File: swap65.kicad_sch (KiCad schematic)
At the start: 0 parts

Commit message: wired up first pass of schematic
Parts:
- added C1, C15, C16, C7: 1uF, symbol Device:C_Small
- added C10, C11, C12, C13, C14, C17, C2, C5, C8, C9: 100nF, symbol Device:C_Small
- added C3, C4: 22pF, symbol Device:C_Small
- added C6: 10uF, symbol Device:C_Small
- added F1: 500mA, symbol Device:Polyfuse_Small
- added J1: SWD, symbol Connector_Generic:Conn_01x05
- added J2: USB_C_Receptacle_USB2.0, symbol Connector:USB_C_Receptacle_USB2.0
- added R1, R2: 27R, symbol Device:R_Small
- added R3, R4, R5, R8: 1k, symbol Device:R_Small
- added R6, R7: 5k1, symbol Device:R_Small
- added SW1: SW_Push, symbol Switch:SW_Push
- added U1: RP2040, Package_DFN_QFN:QFN-56-1EP_7x7mm_P0.4mm_EP3.2x3.2mm, symbol MCU_RaspberryPi:RP2040
- added U2: USBLC6-2SC6, Package_TO_SOT_SMD:SOT-23-6, symbol Power_Protection:USBLC6-2SC6
- added U3: XC6206PxxxMR, Package_TO_SOT_SMD:SOT-23-3, symbol Regulator_Linear:XC6206PxxxMR
- added U4: W25Q128JVS, Package_SO:SOIC-8_5.23x5.23mm_P1.27mm, symbol Memory_Flash:W25Q128JVS
- added Y1: 12MHz, symbol Device:Crystal_GND24_Small
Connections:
- new net: C4.2, R4.1, Y1.1
- new net: C3.2, U1.20 (XIN), Y1.3
- new net: J2.S1 (SHIELD), R5.2
- new net: R4.2, U1.21 (XOUT)
- new net +1V1: C1.1, C2.1, C5.1, U1.23 (DVDD), U1.45 (VREG_VOUT), U1.50 (DVDD)
- new net +3V3: C10.1, C11.1, C12.1, C13.1, C14.1, C16.2, C17.1, C6.1, C7.1, C8.1, C9.1, J1.2 (Pin_2), R3.1, U1.1 (IOVDD), U1.10 (IOVDD), U1.22 (IOVDD), U1.33 (IOVDD), U1.42 (IOVDD), U1.43 (ADC_AVDD), U1.44 (VREG_IN), U1.48 (USB_VDD), U1.49 (IOVDD), U3.2 (VO), U4.8 (VCC)
- new net +5V: C15.2, F1.2, U2.5 (VBUS), U3.3 (VI)
- new net CC1: J2.A5 (CC1), R6.1
- new net CC2: J2.B5 (CC2), R7.1
- new net CS: R8.2, U1.56 (QSPI_SS), U4.1 (~{CS})
- new net D_+: R1.2, U1.47 (USB_DP)
- new net D_-: R2.2, U1.46 (USB_DM)
- new net D_N: R2.1, U2.3 (I/O2)
- new net D_P: R1.1, U2.1 (I/O1)
- new net D_USB_N: J2.A7 (D-), J2.B7 (D-), U2.4 (I/O2)
- new net D_USB_P: J2.A6 (D+), J2.B6 (D+), U2.6 (I/O1)
- new net GND: C1.2, C10.2, C11.2, C12.2, C13.2, C14.2, C15.1, C16.1, C17.2, C2.2, C3.1, C4.1, C5.2, C6.2, C7.2, C8.2, C9.2, J1.3 (Pin_3), J2.A1 (GND), J2.A12 (GND), J2.B1 (GND), J2.B12 (GND), R5.1, R6.2, R7.2, SW1.1, U1.19 (TESTEN), U1.57 (GND), U2.2 (GND), U3.1 (GND), U4.4 (GND), Y1.2, Y1.4
- new net QSPI_CLK: U1.52 (QSPI_SCLK), U4.6 (CLK)
- new net RESET: J1.1 (Pin_1), R3.2, U1.26 (RUN)
- new net SD0: U1.53 (QSPI_SD0), U4.5 (DI(IO0))
- new net SD1: U1.55 (QSPI_SD1), U4.2 (DO(IO1))
- new net SD2: U1.54 (QSPI_SD2), U4.3 (IO2)
- new net SD3: U1.51 (QSPI_SD3), U4.7 (IO3)
- new net SWCLK: J1.5 (Pin_5), U1.24 (SWCLK)
- new net SWD: J1.4 (Pin_4), U1.25 (SWD)
- new net USB_BOOT: R8.1, SW1.2
- new net VBUS: F1.1, J2.A4 (VBUS), J2.A9 (VBUS), J2.B4 (VBUS), J2.B9 (VBUS)
- no-connect marks 0 -> 2
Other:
- added sheet matrix (matrix.kicad_sch)
- title: (none) -> Swap 65 PCB

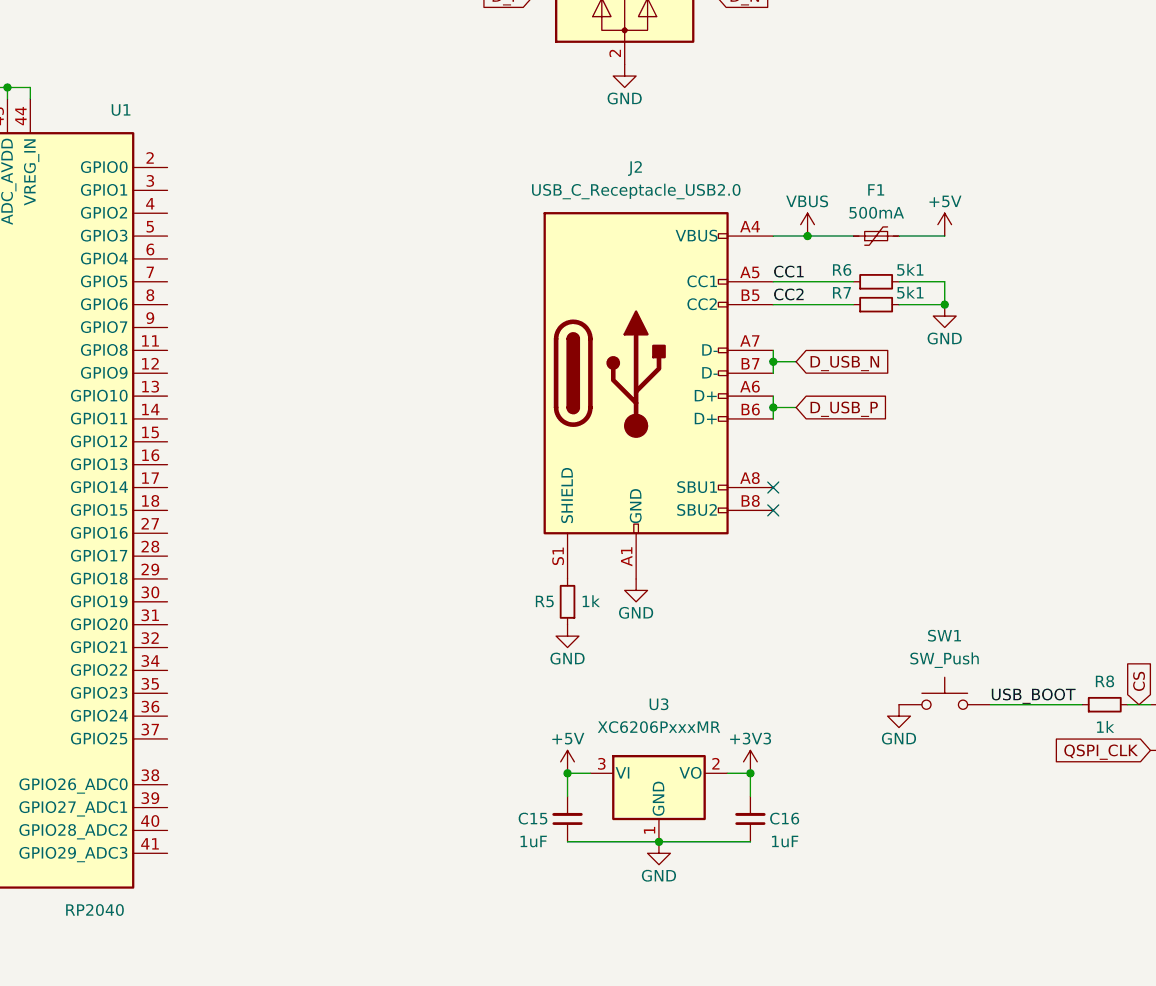
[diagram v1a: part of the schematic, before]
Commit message: did initial routing of MCU and USB
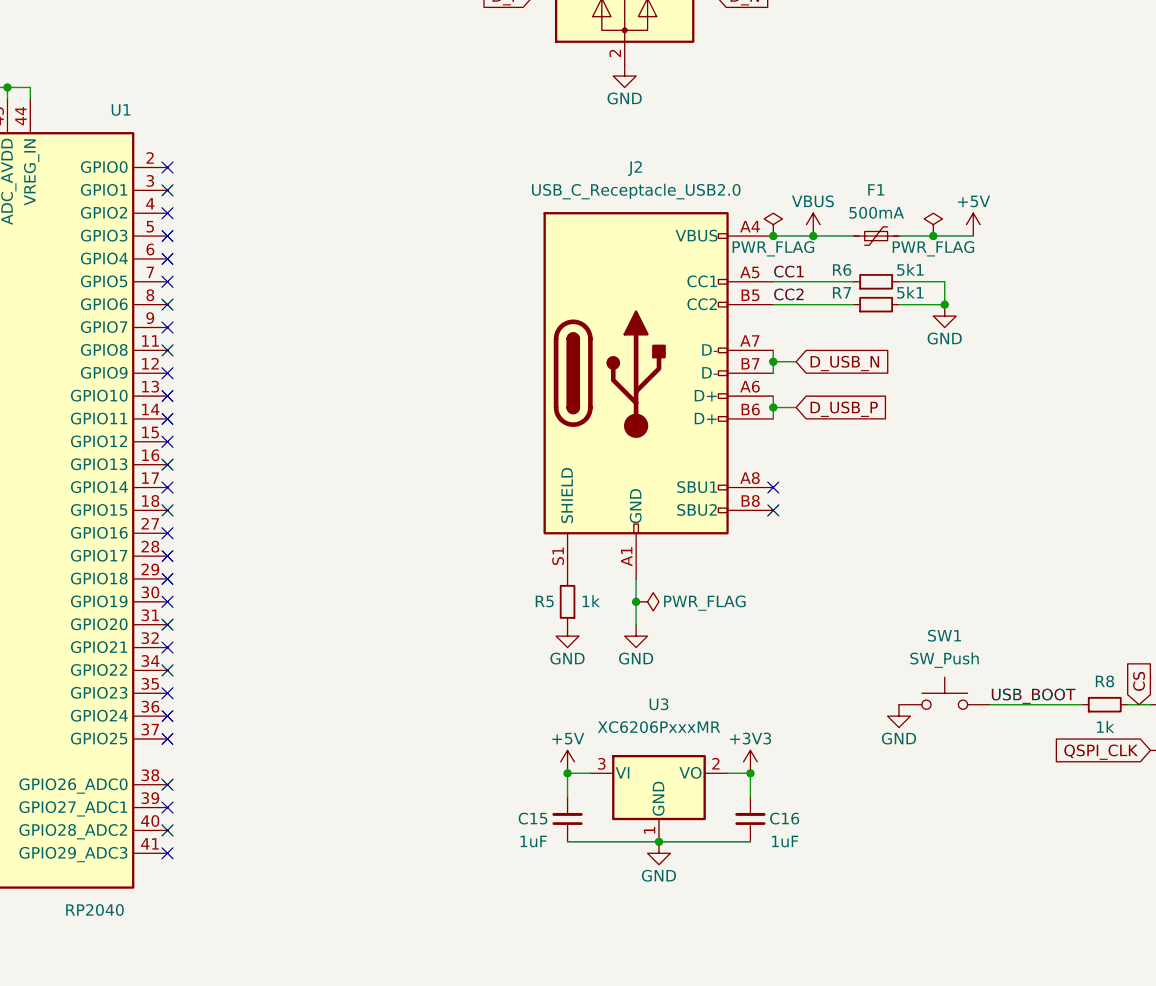
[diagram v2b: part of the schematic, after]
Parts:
- C1, C10, C11, C12, C13, C14, C15, C16, C17, C2, C3, C4, C5, C6, C7, C8, C9: footprint (none) -> Capacitor_SMD:C_0402_1005Metric_Pad0.74x0.62mm_HandSolder
- F1: footprint (none) -> Fuse:Fuse_0805_2012Metric_Pad1.15x1.40mm_HandSolder
- J1: footprint (none) -> Connector_PinHeader_2.54mm:PinHeader_1x05_P2.54mm_Vertical
- J2: footprint (none) -> Connector_USB:USB_C_Receptacle_HRO_TYPE-C-31-M-12
- R1, R2, R3, R4, R5, R6, R7, R8: footprint (none) -> Resistor_SMD:R_0402_1005Metric_Pad0.72x0.64mm_HandSolder
- SW1: footprint (none) -> Button_Switch_SMD:SW_SPST_SKQG_WithStem
- Y1: footprint (none) -> Crystal:Crystal_SMD_2016-4Pin_2.0x1.6mm
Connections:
- no-connect marks 2 -> 32

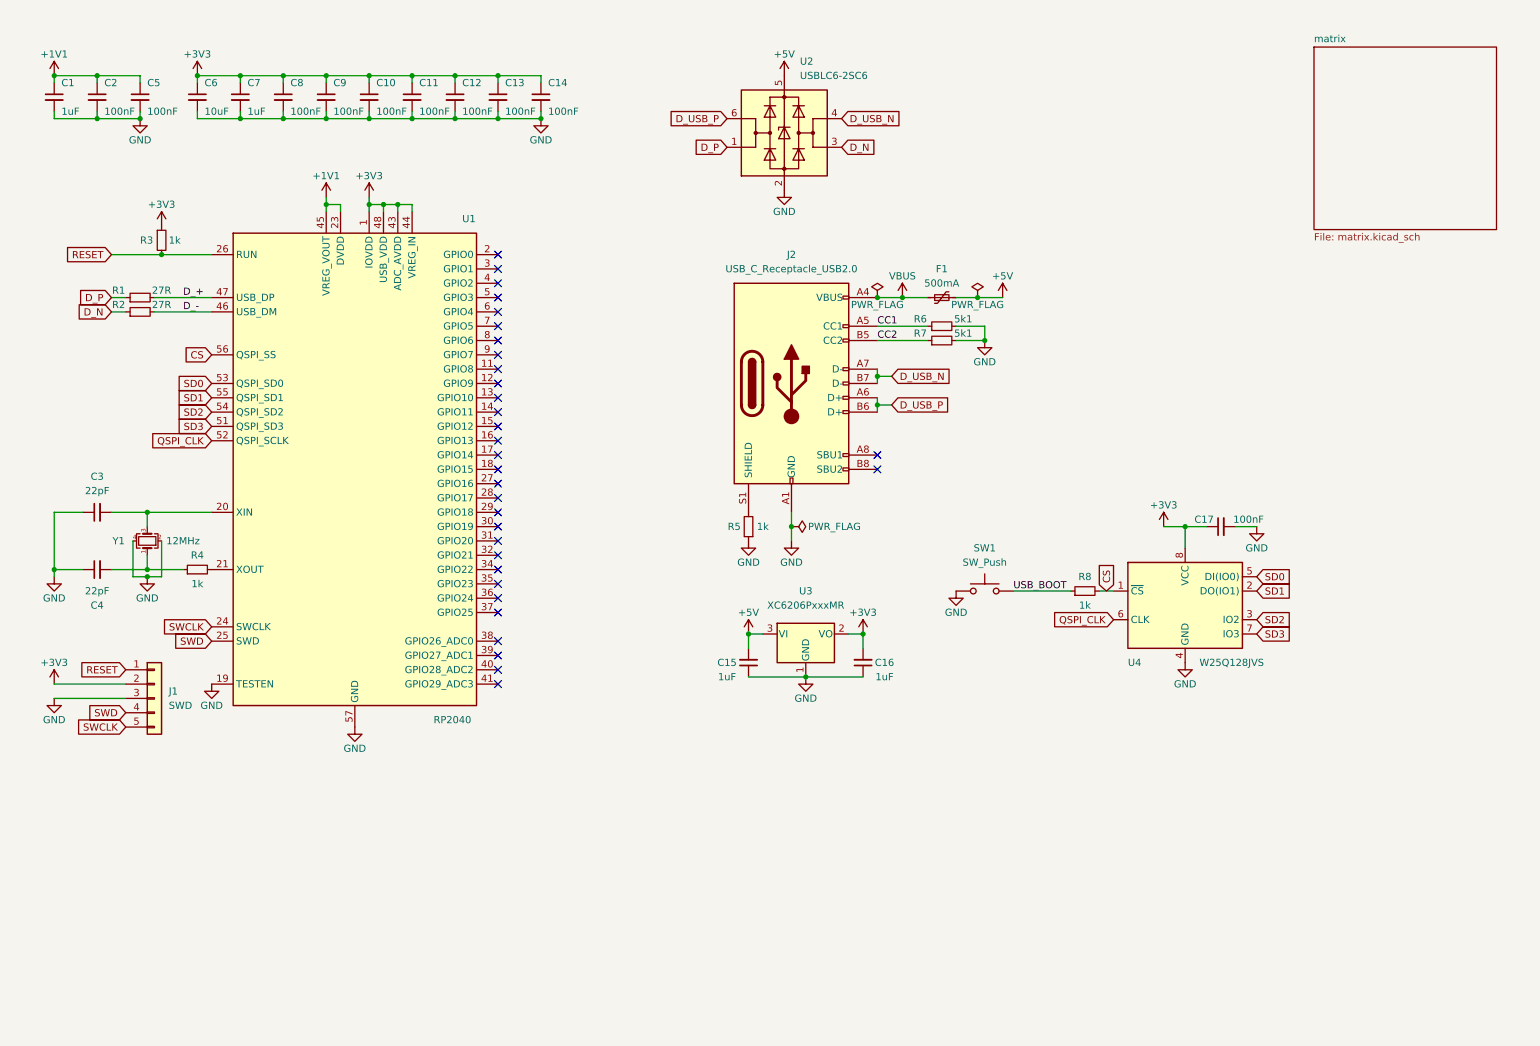
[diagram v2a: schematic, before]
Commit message: routed columns
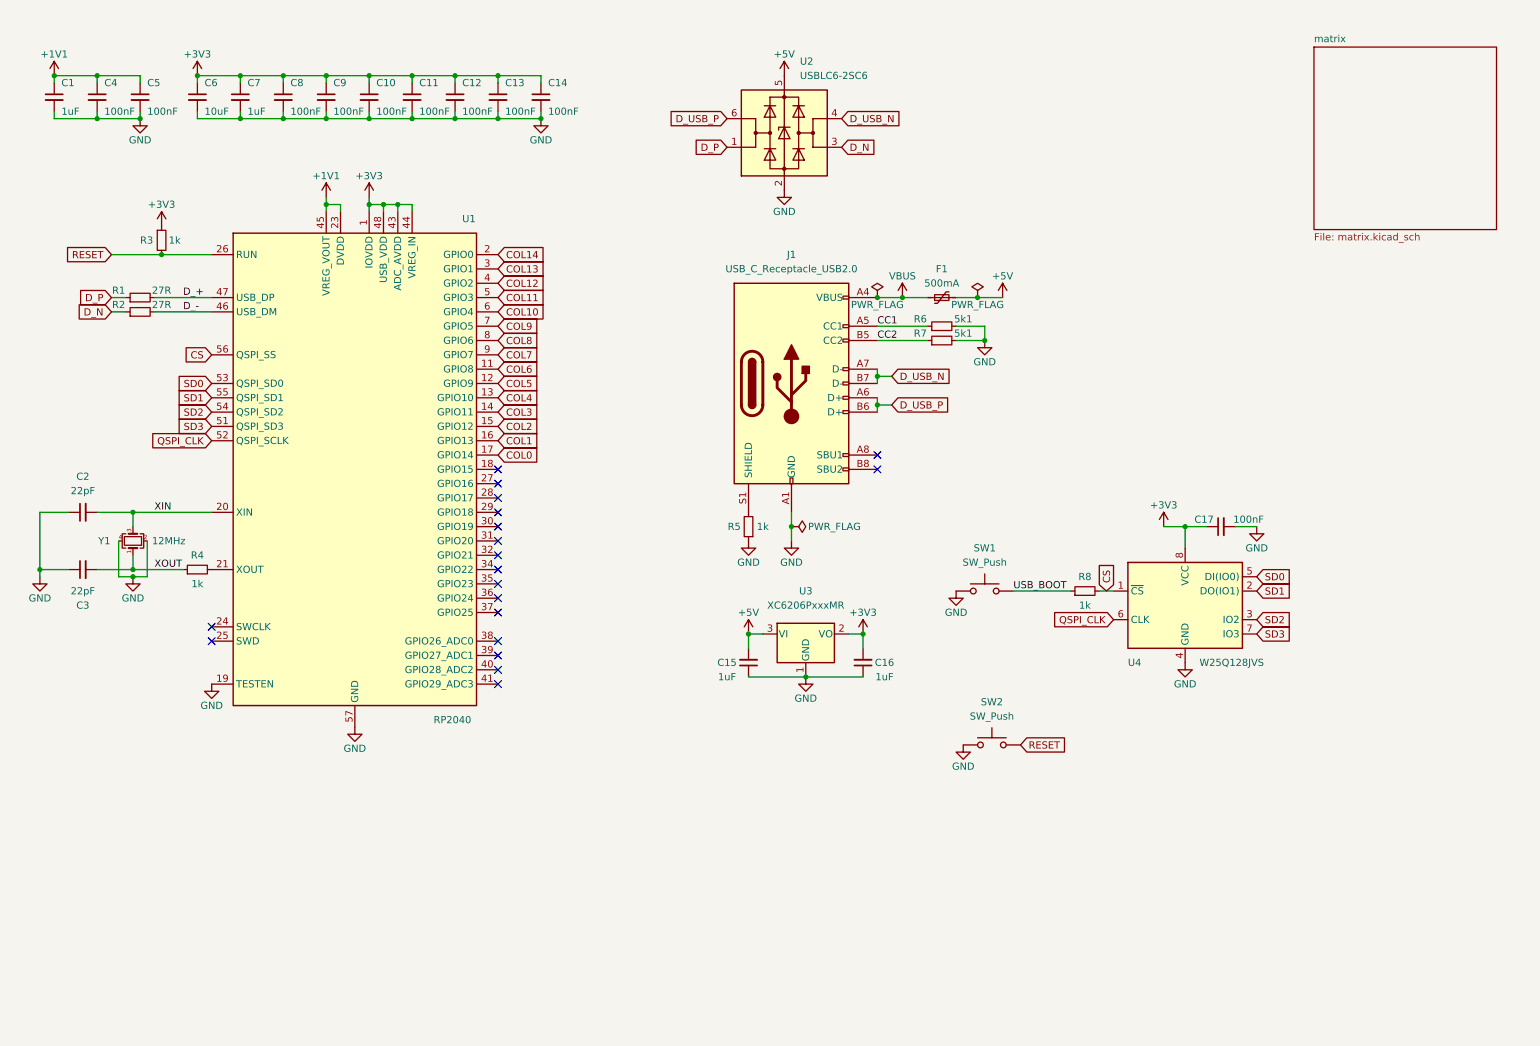
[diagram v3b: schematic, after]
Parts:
- removed J1: SWD, Connector_PinHeader_2.54mm:PinHeader_1x05_P2.54mm_Vertical, symbol Connector_Generic:Conn_01x05
- added SW2: SW_Push, Button_Switch_SMD:SW_SPST_SKQG_WithStem, symbol Switch:SW_Push
- renumbered C3 to C2, C4 to C3, C2 to C4, J2 to J1
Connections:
- net GND: now also SW2.1
- net RESET: now also SW2.2
- net XOUT: now reaches C3.2, R4.1, Y1.1
- net XIN: now reaches C2.2, U1.20 (XIN), Y1.3
- net COL6: now reaches U1.11 (GPIO8)
- net COL5: now reaches U1.12 (GPIO9)
- net COL4: now reaches U1.13 (GPIO10)
- net COL3: now reaches U1.14 (GPIO11)
- net COL2: now reaches U1.15 (GPIO12)
- net COL1: now reaches U1.16 (GPIO13)
- net COL0: now reaches U1.17 (GPIO14)
- net COL14: now reaches U1.2 (GPIO0)
- net COL13: now reaches U1.3 (GPIO1)
- net COL12: now reaches U1.4 (GPIO2)
- net COL11: now reaches U1.5 (GPIO3)
- net COL10: now reaches U1.6 (GPIO4)
- net COL9: now reaches U1.7 (GPIO5)
- net COL8: now reaches U1.8 (GPIO6)
- net COL7: now reaches U1.9 (GPIO7)
- net SWCLK: no longer names the net of U1.24 (SWCLK)
- net SWD: no longer names the net of U1.25 (SWD)
- no-connect marks 32 -> 19
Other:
- moved on the sheet: C2, C3, Y1

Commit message: completed first pass at routing
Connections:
- net ROW4: now reaches U1.29 (GPIO18)
- net ROW3: now reaches U1.30 (GPIO19)
- net ROW2: now reaches U1.31 (GPIO20)
- net ROW1: now reaches U1.35 (GPIO23)
- net ROW0: now reaches U1.36 (GPIO24)
- no-connect marks 19 -> 14
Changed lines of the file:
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@@
   (no_connect (at 100.33 113.03))
   (no_connect (at 100.33 120.65))
-  (no_connect (at 100.33 118.11))
   (no_connect (at 167.64 95.25))
   (no_connect (at 100.33 97.79))
   (no_connect (at 100.33 125.73))
-  (no_connect (at 100.33 105.41))
-  (no_connect (at 100.33 102.87))
   (no_connect (at 100.33 95.25))
   (no_connect (at 100.33 133.35))
@@
   (no_connect (at 100.33 128.27))
   (no_connect (at 49.53 125.73))
-  (no_connect (at 100.33 107.95))
-  (no_connect (at 100.33 115.57))
   (wire (pts (xy 165.1 124.46) (xy 165.1 127))
     (stroke (width 0) (type default) (color 0 0 0 0))
@@
     )
   )
+  (global_label "ROW3" (shape input) (at 100.33 105.41 0) (fields_autoplaced)
+    (effects (font (size 1.27 1.27)) (justify left))
+    (property "Intersheet References" "${INTERSHEET_REFS}" (id 0) (at 108.0045 105.3306 0)
+      (effects (font (size 1.27 1.27)) (justify left) hide)
+    )
+  )
   (global_label "QSPI_CLK" (shape input) (at 209.55 121.92 180) (fields_autoplaced)
     (effects (font (size 1.27 1.27)) (justify right))
@@
     )
   )
+  (global_label "ROW1" (shape input) (at 100.33 115.57 0) (fields_autoplaced)
+    (effects (font (size 1.27 1.27)) (justify left))
+    (property "Intersheet References" "${INTERSHEET_REFS}" (id 0) (at 108.0045 115.4906 0)
+      (effects (font (size 1.27 1.27)) (justify left) hide)
+    )
+  )
   (global_label "SD3" (shape input) (at 49.53 87.63 180) (fields_autoplaced)
     (effects (font (size 1.27 1.27)) (justify right))
@@
     )
   )
+  (global_label "ROW4" (shape input) (at 100.33 102.87 0) (fields_autoplaced)
+    (effects (font (size 1.27 1.27)) (justify left))
+    (property "Intersheet References" "${INTERSHEET_REFS}" (id 0) (at 108.0045 102.7906 0)
+      (effects (font (size 1.27 1.27)) (justify left) hide)
+    )
+  )
   (global_label "COL1" (shape input) (at 100.33 90.17 0) (fields_autoplaced)
     (effects (font (size 1.27 1.27)) (justify left))
@@
     )
   )
+  (global_label "ROW0" (shape input) (at 100.33 118.11 0) (fields_autoplaced)
+    (effects (font (size 1.27 1.27)) (justify left))
+    (property "Intersheet References" "${INTERSHEET_REFS}" (id 0) (at 108.0045 118.0306 0)
+      (effects (font (size 1.27 1.27)) (justify left) hide)
+    )
+  )
   (global_label "D_USB_P" (shape input) (at 170.18 83.82 0) (fields_autoplaced)
     (effects (font (size 1.27 1.27)) (justify left))
@@
       (effects (font (size 1.27 1.27)) (justify left) hide)
     )
+  )
+  (global_label "ROW2" (shape input) (at 100.33 107.95 0) (fields_autoplaced)
+    (effects (font (size 1.27 1.27)) (justify left))
+    (property "Intersheet References" "${INTERSHEET_REFS}" (id 0) (at 108.0045 107.8706 0)
+      (effects (font (size 1.27 1.27)) (justify left) hide)
+    )
